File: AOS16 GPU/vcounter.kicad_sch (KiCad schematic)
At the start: 22 parts, among them U10 74LS30, U11 74LS30, U12 74HC00, U13 74AHC04, U14 74LS30, U15 74LS30, U16 74LS30, U17 74LS30, U4 74LS161, U5 74LS161, U6 74AHC04, U7 74AHC04, U8 74LS30, U9 74LS30

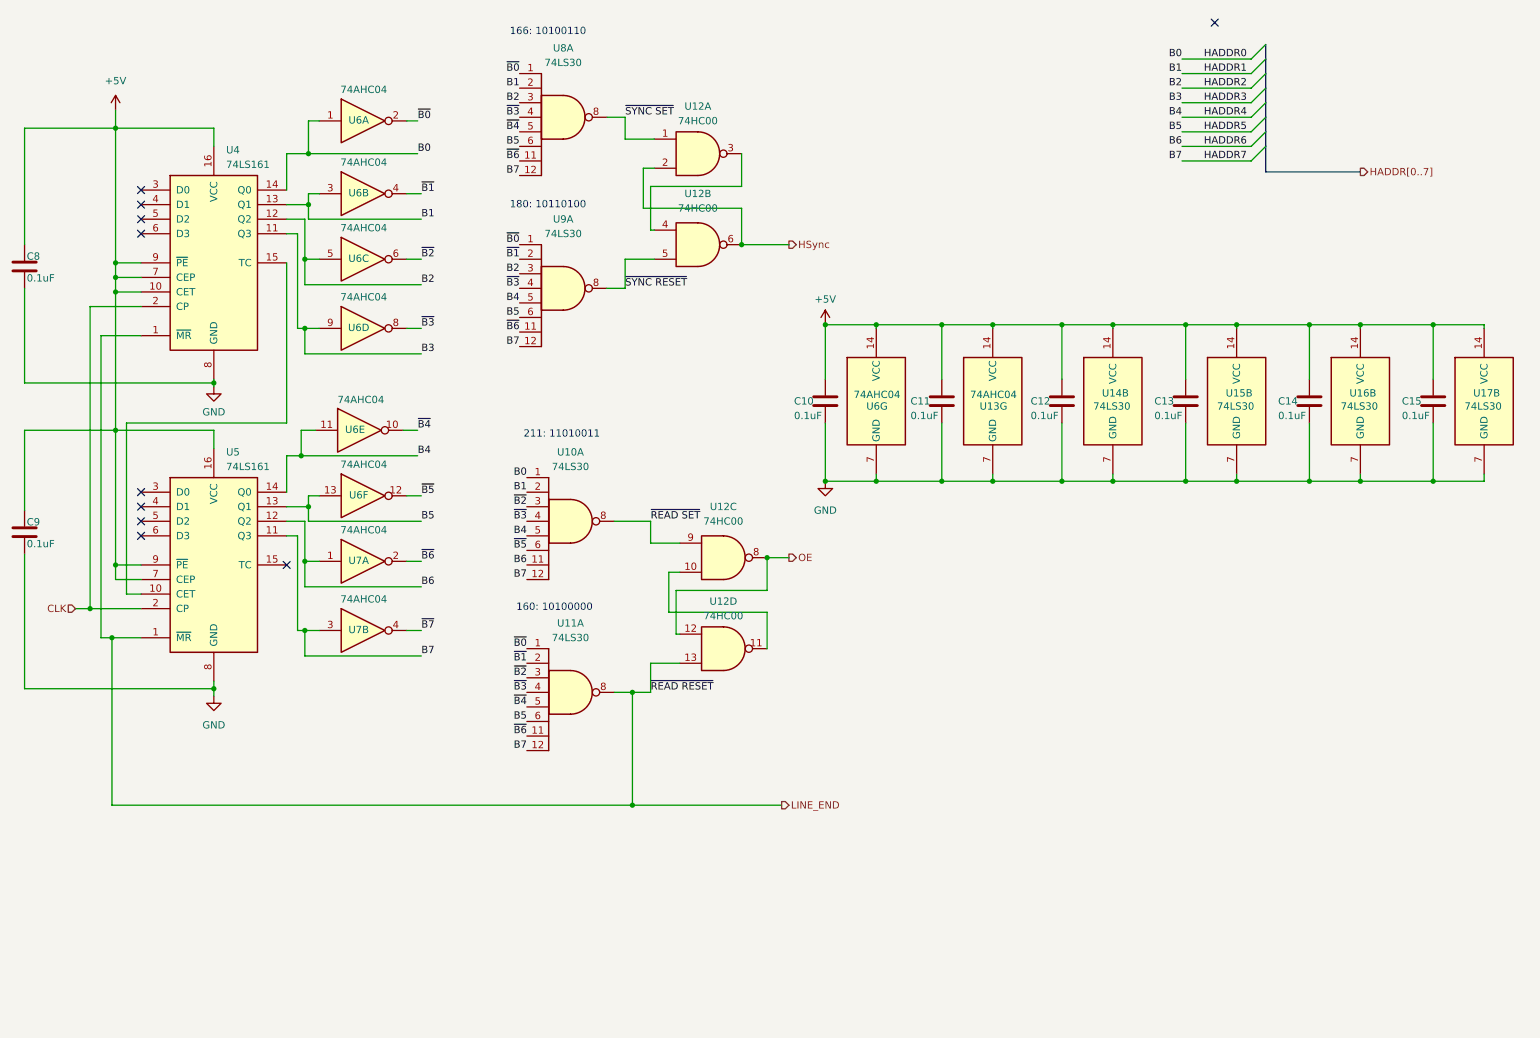
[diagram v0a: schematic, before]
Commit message: Completed GPU schematic
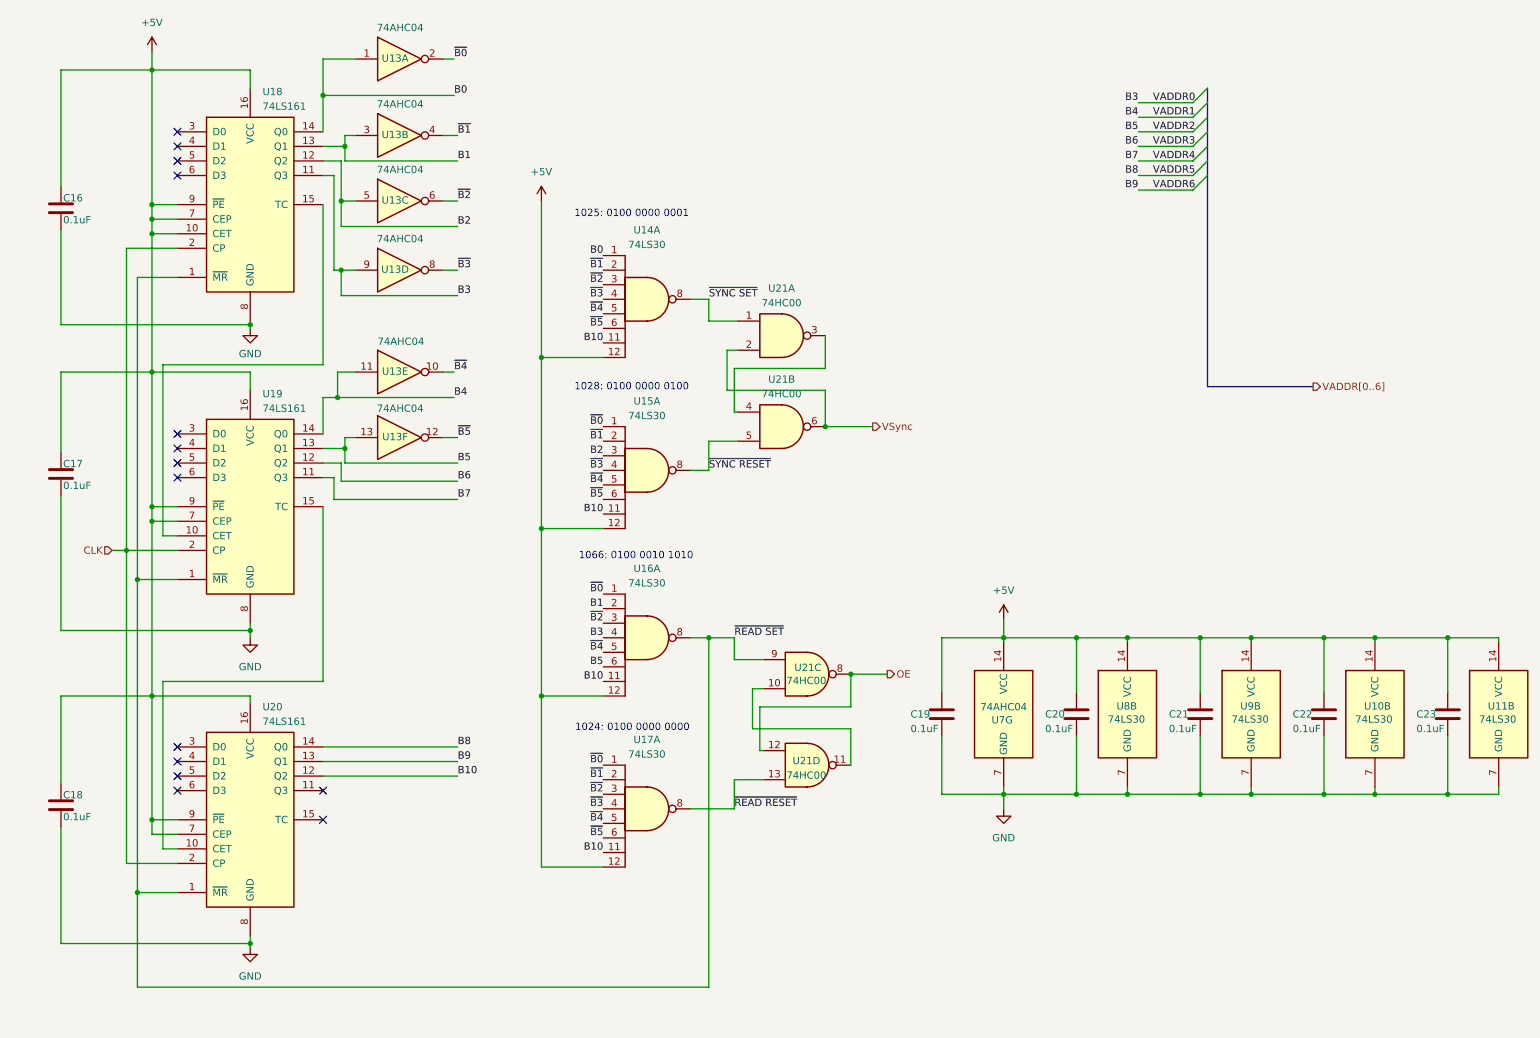
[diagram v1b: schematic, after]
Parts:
- removed C10, C11, C12, C13, C14, C15, C8, C9: 0.1uF, Capacitor_SMD:C_0603_1608Metric, symbol Device:C
- removed U10, U11, U14, U15, U16, U17, U8, U9: 74LS30, Package_SO:SOIC-14_3.9x8.7mm_P1.27mm, symbol 74xx:74LS30
- removed U12: 74HC00, Package_SO:SOIC-14_3.9x8.7mm_P1.27mm, symbol 74xx:74HC00
- removed U13, U6, U7: 74AHC04, Package_SO:SOIC-14_3.9x8.7mm_P1.27mm, symbol 74xx:74AHC04
- removed U4, U5: 74LS161, Package_SO:SOIC-16_3.9x9.9mm_P1.27mm, symbol 74xx:74LS161
- added C16, C17, C18, C19, C20, C21, C22, C23: 0.1uF, Capacitor_SMD:C_0603_1608Metric, symbol Device:C
- added U10, U11, U14, U15, U16, U17, U8, U9: 74LS30, Package_SO:SOIC-14_3.9x8.7mm_P1.27mm, symbol 74xx:74LS30
- added U13, U7: 74AHC04, Package_SO:SOIC-14_3.9x8.7mm_P1.27mm, symbol 74xx:74AHC04
- added U18, U19, U20: 74LS161, Package_SO:SOIC-16_3.9x9.9mm_P1.27mm, symbol 74xx:74LS161
- added U21: 74HC00, Package_SO:SOIC-14_3.9x8.7mm_P1.27mm, symbol 74xx:74HC00
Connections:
- net +5V: now also C16.1, C17.1, C18.1, C19.1, C20.1, C21.1, C22.1, C23.1, U10.14 (VCC), U11.14 (VCC), U14.12, U15.12, U16.12, U17.12, U18.10 (CET), U18.16 (VCC), U18.7 (CEP), U18.9 (~{PE}), U19.16 (VCC), U19.7 (CEP), U19.9 (~{PE}), U20.16 (VCC), U20.7 (CEP), U20.9 (~{PE}), U7.14 (VCC), U8.14 (VCC), U9.14 (VCC)
- net B0: now also U13.1, U14.1, U18.14 (Q0)
- net B1: now also U13.3, U16.2, U18.13 (Q1)
- net B2: now also U13.5, U15.3, U18.12 (Q2)
- net B3: now also U13.9, U16.4, U18.11 (Q3)
- net B4: now also U13.11, U19.14 (Q0)
- net B5: now also U13.13, U16.6, U19.13 (Q1)
- net B6: now also U19.12 (Q2)
- net B7: now also U19.11 (Q3)
- net CLK: now also U18.2 (CP), U19.2 (CP), U20.2 (CP)
- net GND: now also C16.2, C17.2, C18.2, C19.2, C20.2, C21.2, C22.2, C23.2, U10.7 (GND), U11.7 (GND), U18.8 (GND), U19.8 (GND), U20.8 (GND), U7.7 (GND), U8.7 (GND), U9.7 (GND)
- net OE: now also U21.12, U21.8
- net ~{B0}: now also U13.2, U15.1, U16.1, U17.1
- net ~{B1}: now also U13.4, U14.2, U15.2, U17.2
- net ~{B2}: now also U13.6, U14.3, U16.3, U17.3
- net ~{B3}: now also U13.8, U14.4, U15.4, U17.4
- net ~{B4}: now also U13.10, U14.5, U15.5, U16.5, U17.5
- net ~{B5}: now also U13.12, U14.6, U15.6, U17.6
- net ~{READ SET}: now also U16.8, U18.1 (~{MR}), U19.1 (~{MR}), U20.1 (~{MR}), U21.9
- net ~{SYNC RESET}: now also U15.8, U21.5
- net ~{SYNC SET}: now also U14.8, U21.1
- new net: U21.10, U21.11
- new net: U19.15 (TC), U20.10 (CET)
- new net: U18.15 (TC), U19.10 (CET)
- new net: U21.3, U21.4
- new net B10: U14.11, U15.11, U16.11, U17.11, U20.12 (Q2)
- new net B8: U20.14 (Q0)
- new net B9: U20.13 (Q1)
- new net VSync: U21.2, U21.6
- new net ~{READ RESET}: U17.8, U21.13
- no-connect marks 10 -> 14
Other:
- note added: "1024: 0100 0000 0000"
- note added: "1025: 0100 0000 0001"
- note added: "1028: 0100 0000 0100"
- note added: "1066: 0100 0010 1010"
- note removed: "160: 10100000"
- note removed: "166: 10100110"
- note removed: "180: 10110100"
- note removed: "211: 11010011"

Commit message: GPU PCB Design v1
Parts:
- removed unit 2 of U13
- removed unit 6 of U13
- added C26: 0.1uF, Capacitor_SMD:C_0603_1608Metric, symbol Device:C
- added unit 2 of U12
- added U20: 74LS21, Package_SO:SOIC-14_3.9x8.7mm_P1.27mm, symbol 74xx:74LS21
- renumbered C16 to C15, C17 to C16, C18 to C17, C19 to C18, C20 to C19, C21 to C20, C22 to C21, C23 to C22, U11 to U10, U13 to U12, U14 to U13, U15 to U14, U16 to U15, U17 to U16, U18 to U17, U19 to U18, U20 to U19, U7 to U5, U8 to U7, U9 to U8, U10 to U9
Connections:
- net +5V: now also C26.1, U20.14 (VCC); no longer U13.12, U14.12, U15.12, U16.12
- net B0: now also U15.1; no longer U13.1
- net B1: now also U12.3; no longer U15.2
- net B2: now also U14.1, U15.5; no longer U14.3
- net B3: now also U12.9, U15.3; no longer U12.9, U15.4
- net B4: now also U12.11, U15.2; no longer U12.11
- net B5: now also U20.2; no longer U15.6
- net B6: now also U20.4
- net B7: now also U20.5
- net B8: now also U20.1
- net GND: now also C26.2, U20.7 (GND)
- net ~{B0}: now also U13.6, U14.2; no longer U14.1, U15.1
- net ~{B1}: now also U13.5, U14.3, U12.4; no longer U13.2, U14.2
- net ~{B2}: now also U16.4; no longer U15.3, U16.3
- net ~{B3}: now also U12.8, U16.3; no longer U12.8, U16.4
- net ~{B4}: now also U12.10, U13.1, U14.6; no longer U12.10, U13.5, U14.5, U15.5
- removed net B10: U13.11, U14.11, U15.11, U16.11, U19.12 (Q2)
- net B9: no longer names the net of U19.13 (Q1)
- removed net ~{B5}: U13.6, U14.6, U16.6
- new net: U13.2, U14.5, U15.4, U16.6, U20.6
- no-connect marks 14 -> 25
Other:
- note added: "480: 0001 1110 0000"
- note added: "481: 0001 1110 0001"
- note added: "484: 0001 1110 0100"
- note added: "509: 0001 1111 1101"
- note removed: "1024: 0100 0000 0000"
- note removed: "1025: 0100 0000 0001"
- note removed: "1028: 0100 0000 0100"
- note removed: "1066: 0100 0010 1010"
- moved on the sheet: U12D, U12E, U13A, U14A, U15A, U16A, U21A, U21B, U21C, U21D

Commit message: updated gpu
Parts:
- added D3, D6: LED_Small, LED_SMD:LED_0603_1608Metric, symbol Device:LED_Small
- added R3, R42: 220, Resistor_SMD:R_0603_1608Metric, symbol Device:R_Small
- added TP11: NEW FRAME, TestPoint:TestPoint_Pad_D2.0mm, symbol Connector:TestPoint
- U13: renamed from U7; value 74LS30 -> 74HC30
- U13, U14, U15, U16: value 74LS30 -> 74HC30
- U14: renamed from U8; value 74LS30 -> 74HC30
- U15: renamed from U9; value 74LS30 -> 74HC30
- U16: renamed from U10; value 74LS30 -> 74HC30
- U17, U18, U19: value 74LS161 -> 74HC161
- U20: value 74LS21 -> 74HC21
- renumbered U5 to U12
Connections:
- net +5V: now also U13.11, U13.12, U14.11, U14.12, U15.11, U15.12, U16.11, U16.12
- net B0: now also U13.6
- net GND: now also U17.3 (D0), U17.4 (D1), U17.5 (D2), U17.6 (D3), U18.3 (D0), U18.4 (D1), U18.5 (D2), U18.6 (D3), U19.3 (D0), U19.4 (D1), U19.5 (D2), U19.6 (D3), D3.1 (K), D6.1 (K)
- net VSync: now also R42.1
- net ~{B0}: no longer U13.6
- net ~{B1}: now also U15.6
- net ~{READ SET}: now also R3.1, TP11.1
- new net: D3.2 (A), R3.2
- new net: D6.2 (A), R42.2
- no-connect marks 25 -> 4
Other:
- moved on the sheet: C15, C16, C17
